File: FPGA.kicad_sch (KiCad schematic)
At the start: 1 part, among them U2 LFE5U-85F-6BG381x

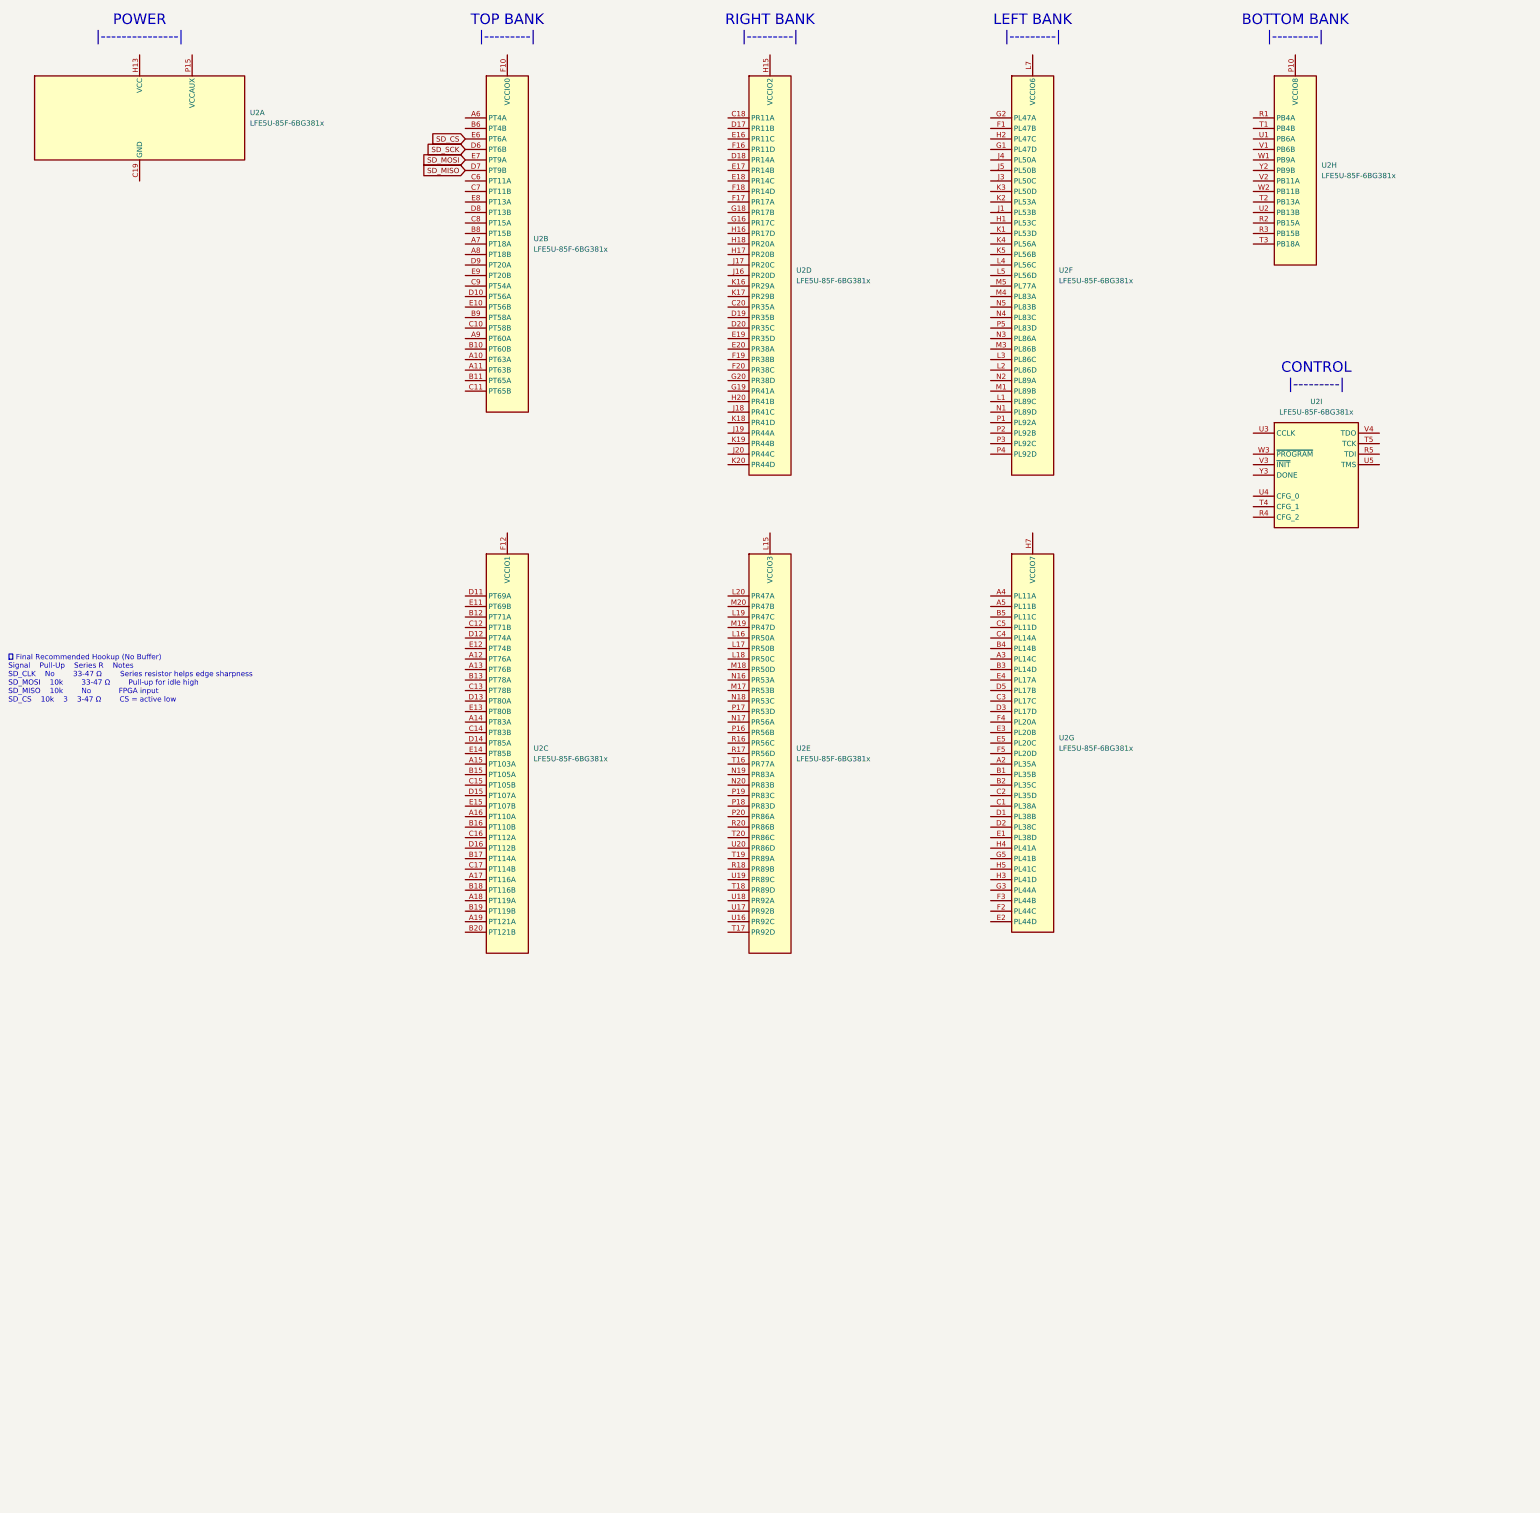
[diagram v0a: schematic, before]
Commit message: Changed power regulators, filled out DRAM, begin changing FPGA from ECP5 to ICE40
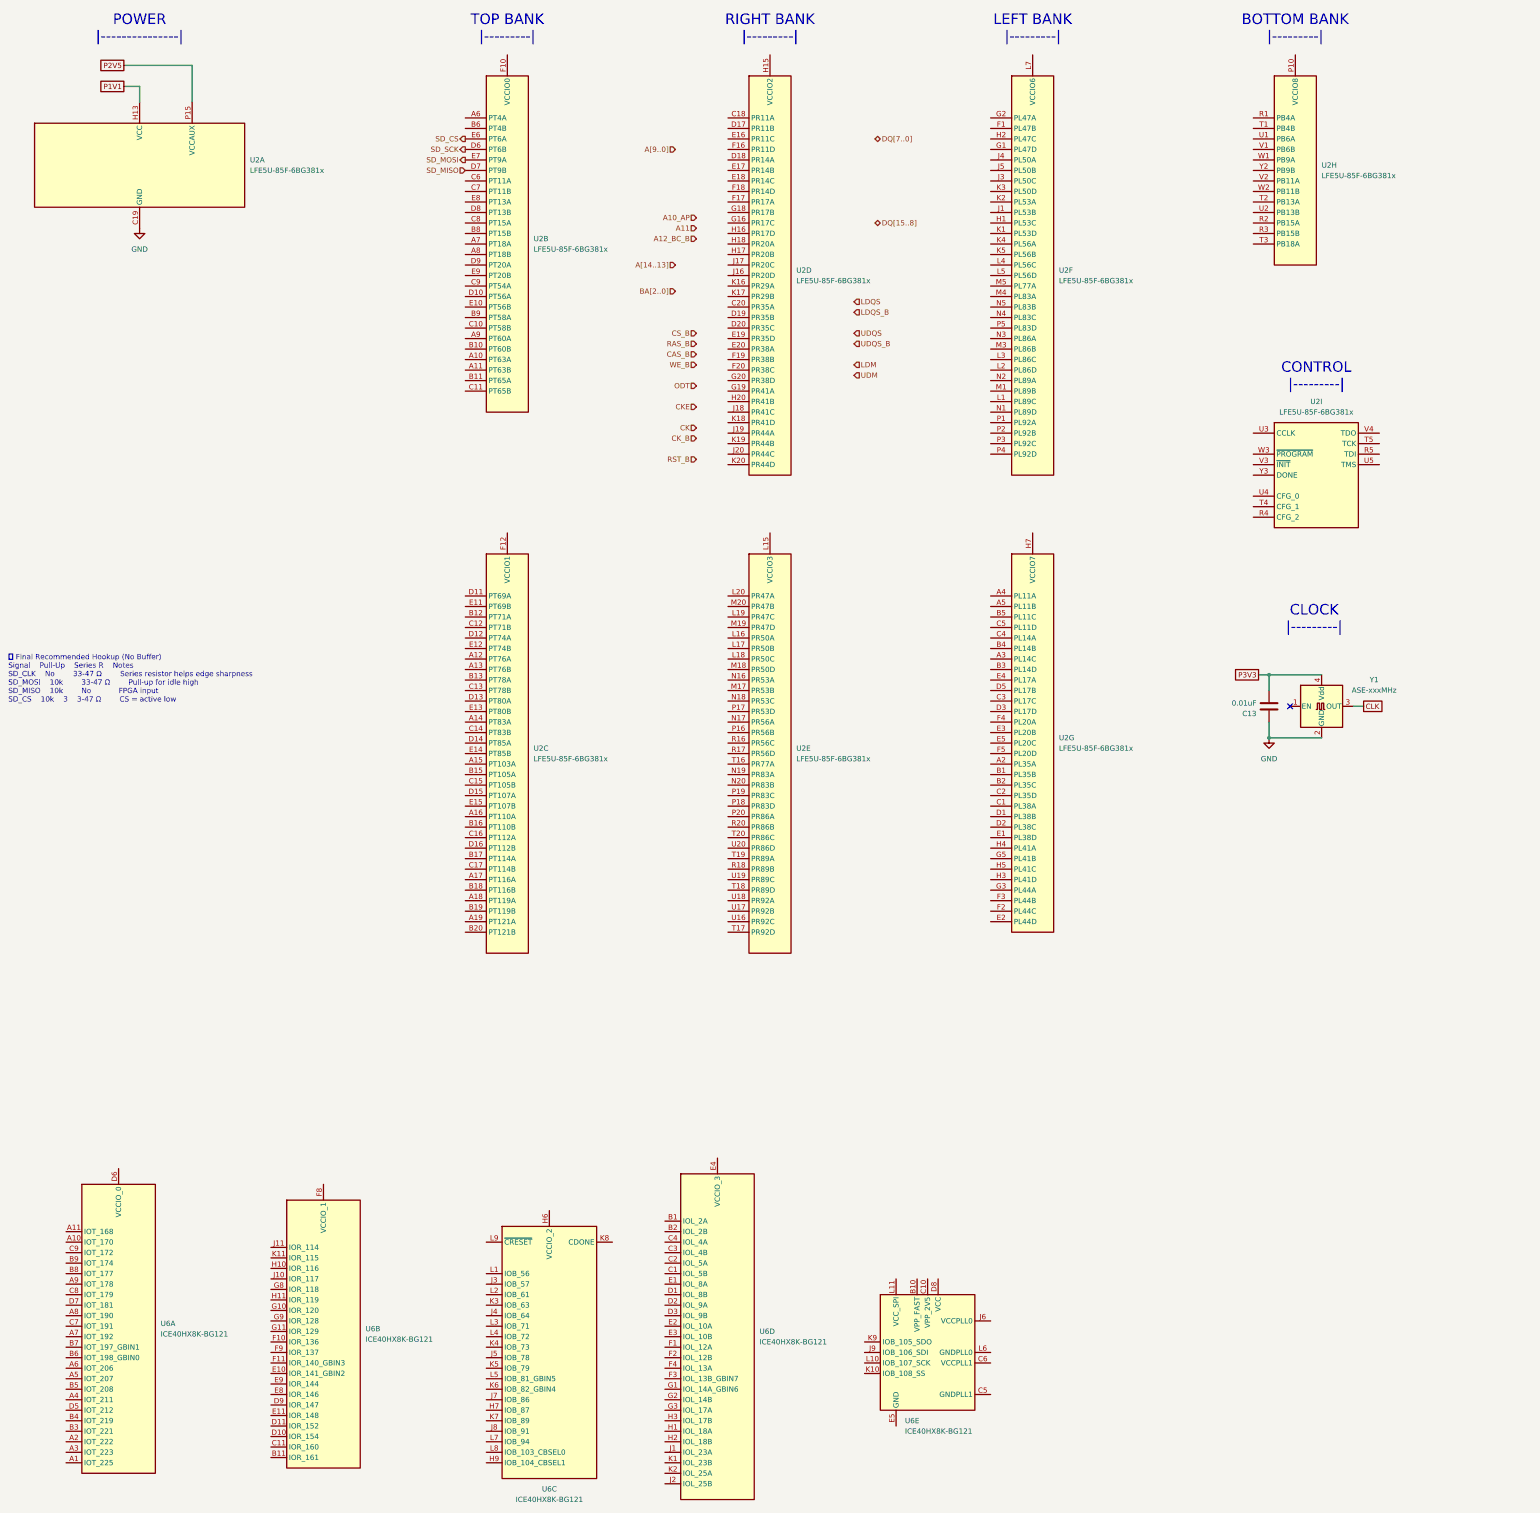
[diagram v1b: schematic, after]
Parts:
- added C13: 0.01uF, symbol Device:C
- added U6: ICE40HX8K-BG121, Package_BGA:BGA-121_9.0x9.0mm_Layout11x11_P0.8mm_Ball0.4mm_Pad0.35mm_NSMD, symbol FPGA_Lattice:ICE40HX8K-BG121
- added Y1: ASE-xxxMHz, Oscillator:Oscillator_SMD_Abracon_ASE-4Pin_3.2x2.5mm, symbol Oscillator:ASE-xxxMHz
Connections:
- net GND: now reaches U2.B14 (GND), U2.B7 (GND), U2.C19 (GND), U2.D4 (GND), U2.F13 (GND), U2.F14 (GND), U2.F7 (GND), U2.F8 (GND), U2.G10 (GND), U2.G11 (GND), U2.G12 (GND), U2.G13 (GND), U2.G14 (GND), U2.G15 (GND), U2.G17 (GND), U2.G4 (GND), U2.G6 (GND), U2.G7 (GND), U2.G8 (GND), U2.G9 (GND), U2.H19 (GND), U2.J10 (GND), U2.J11 (GND), U2.J12 (GND), U2.J14 (GND), U2.J2 (GND), U2.J7 (GND), U2.J9 (GND), U2.K10 (GND), U2.K11 (GND), U2.K12 (GND), U2.K14 (GND), U2.K15 (GND), U2.K6 (GND), U2.K7 (GND), U2.K9 (GND), U2.L10 (GND), U2.L11 (GND), U2.L12 (GND), U2.L9 (GND), U2.M10 (GND), U2.M11 (GND), U2.M12 (GND), U2.M14 (GND), U2.M16 (GND), U2.M2 (GND), U2.M7 (GND), U2.M9 (GND), U2.N14 (GND), U2.N15 (GND), U2.N6 (GND), U2.N7 (GND), U2.P11 (GND), U2.P12 (GND), U2.P13 (GND), U2.P14 (GND), U2.P7 (GND), U2.P8 (GND), U2.R19 (GND), U2.T10 (GND), U2.T11 (GND), U2.T12 (GND), U2.T13 (GND), U2.T14 (GND), U2.T15 (GND), U2.T6 (GND), U2.T7 (GND), U2.T8 (GND), U2.T9 (GND), U2.U10 (GND), U2.U11 (GND), U2.U12 (GND), U2.U13 (GND), U2.U14 (GND), U2.U15 (GND), U2.U6 (GND), U2.U7 (GND), U2.U8 (GND), U2.U9 (GND), U2.V10 (GND), U2.V11 (GND), U2.V12 (GND), U2.V13 (GND), U2.V14 (GND), U2.V15 (GND), U2.V16 (GND), U2.V17 (GND), U2.V18 (GND), U2.V19 (GND), U2.V20 (GND), U2.V5 (GND), U2.V6 (GND), U2.V7 (GND), U2.V8 (GND), U2.V9 (GND), U2.W12 (GND), U2.W15 (GND), U2.W16 (GND), U2.W19 (GND), U2.W20 (GND), U2.W6 (GND), U2.W7 (GND), U2.Y11 (GND), U2.Y12 (GND), U2.Y14 (GND), U2.Y15 (GND), U2.Y16 (GND), U2.Y17 (GND), U2.Y19 (GND), U2.Y5 (GND), U2.Y6 (GND), U2.Y7 (GND), U2.Y8 (GND)
- net GND: now also C13.2, Y1.2 (GND)
- net P2V5: now reaches U2.F15 (VCCAUX), U2.F6 (VCCAUX), U2.P15 (VCCAUX), U2.P6 (VCCAUX)
- net P1V1: now reaches U2.H10 (VCC), U2.H11 (VCC), U2.H12 (VCC), U2.H13 (VCC), U2.H8 (VCC), U2.H9 (VCC), U2.J13 (VCC), U2.J8 (VCC), U2.K13 (VCC), U2.K8 (VCC), U2.L13 (VCC), U2.L8 (VCC), U2.M13 (VCC), U2.M8 (VCC), U2.N10 (VCC), U2.N11 (VCC), U2.N12 (VCC), U2.N13 (VCC), U2.N8 (VCC), U2.N9 (VCC)
- new net: U6.E4 (VCCIO_3), U6.G4 (VCCIO_3)
- new net: U6.D4 (VCC), U6.D8 (VCC), U6.H4 (VCC), U6.H8 (VCC)
- new net: U6.E5 (GND), U6.E6 (GND), U6.E7 (GND), U6.F5 (GND), U6.F6 (GND), U6.F7 (GND), U6.G5 (GND), U6.G6 (GND), U6.G7 (GND), U6.H5 (GND)
- new net CLK: Y1.3 (OUT)
- new net P3V3: C13.1, Y1.4 (Vdd)
- no-connect marks 0 -> 1
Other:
- note added: "CLOCK |---------|"
- moved on the sheet: U2A

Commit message: Saving before changing RAM from DDR3 to Parallel SDR SRAM
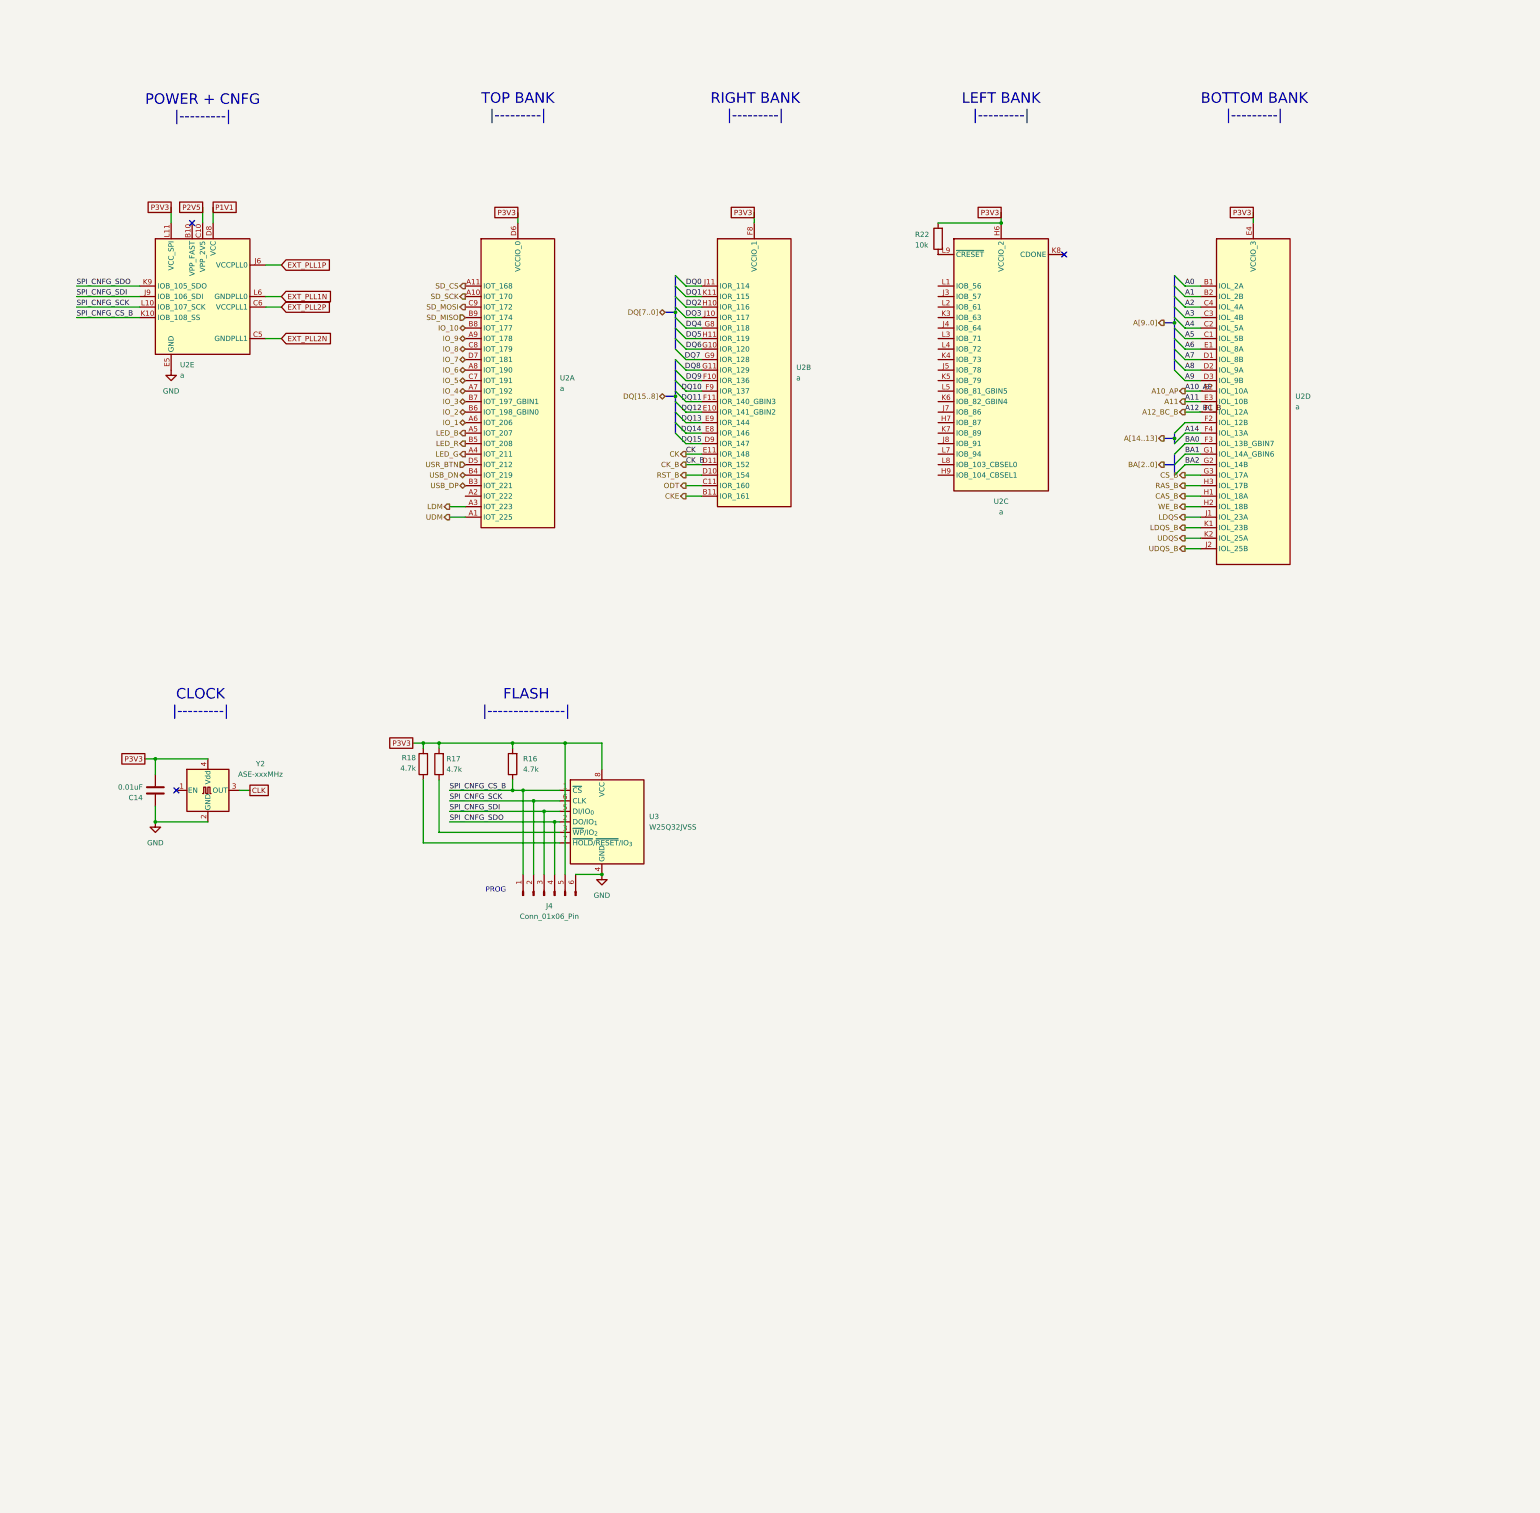
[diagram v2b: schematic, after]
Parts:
- removed U2: LFE5U-85F-6BG381x, Package_BGA:Lattice_caBGA-381_17.0x17.0mm_Layout20x20_P0.8mm_Ball0.4mm_Pad0.4mm_NSMD, symbol FPGA_Lattice:LFE5U-85F-6BG381x
- added J4: Conn_01x06_Pin, symbol Connector:Conn_01x06_Pin
- added R16, R17, R18: 4.7k, symbol Device:R
- added R22: 10k, symbol Device:R
- added U3: W25Q32JVSS, Package_SO:SOIC-8_5.3x5.3mm_P1.27mm, symbol Memory_Flash:W25Q32JVSS
- U2: renamed from U6; value ICE40HX8K-BG121 -> a
- renumbered C13 to C14, Y1 to Y2
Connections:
- net A10_AP: now also U2.E2 (IOL_10A)
- net A11: now also U2.E3 (IOL_10B)
- net A12_BC_B: now also U2.F1 (IOL_12A)
- net CAS_B: now also U2.H1 (IOL_18A)
- net CK: now also U2.E11 (IOR_148)
- net CKE: now also U2.B11 (IOR_161)
- net CK_B: now also U2.D11 (IOR_152)
- net CS_B: now also U2.G3 (IOL_17A)
- net GND: now also U2.E5 (GND), U2.E6 (GND), U2.E7 (GND), U2.F5 (GND), U2.F6 (GND), U2.F7 (GND), U2.G5 (GND), U2.G6 (GND), U2.G7 (GND), U2.H5 (GND), J4.6 (Pin_6), U3.4 (GND)
- net LDM: now also U2.A3 (IOT_223)
- net LDQS: now also U2.J1 (IOL_23A)
- net LDQS_B: now also U2.K1 (IOL_23B)
- net ODT: now also U2.C11 (IOR_160)
- net P1V1: now also U2.D4 (VCC), U2.D8 (VCC), U2.H4 (VCC), U2.H8 (VCC)
- net P2V5: now also U2.C10 (VPP_2V5)
- net P3V3: now also U2.D6 (VCCIO_0), U2.E4 (VCCIO_3), U2.F8 (VCCIO_1), U2.G4 (VCCIO_3), U2.H6 (VCCIO_2), U2.L11 (VCC_SPI), J4.5 (Pin_5), R16.2, R17.2, R18.2, R22.2, U3.8 (VCC)
- net RAS_B: now also U2.H3 (IOL_17B)
- net RST_B: now also U2.D10 (IOR_154)
- net SD_CS: now also U2.A11 (IOT_168)
- net SD_MISO: now also U2.B9 (IOT_174)
- net SD_MOSI: now also U2.C9 (IOT_172)
- net SD_SCK: now also U2.A10 (IOT_170)
- net UDM: now also U2.A1 (IOT_225)
- net UDQS: now also U2.K2 (IOL_25A)
- net UDQS_B: now also U2.J2 (IOL_25B)
- net WE_B: now also U2.H2 (IOL_18B)
- net LED_G: now reaches U2.A4 (IOT_211)
- net LED_B: now reaches U2.A5 (IOT_207)
- net IO_1: now reaches U2.A6 (IOT_206)
- net IO_4: now reaches U2.A7 (IOT_192)
- net IO_6: now reaches U2.A8 (IOT_190)
- net IO_9: now reaches U2.A9 (IOT_178)
- net USB_DP: now reaches U2.B3 (IOT_221)
- net USB_DN: now reaches U2.B4 (IOT_219)
- net LED_R: now reaches U2.B5 (IOT_208)
- net IO_2: now reaches U2.B6 (IOT_198_GBIN0)
- net IO_3: now reaches U2.B7 (IOT_197_GBIN1)
- net IO_10: now reaches U2.B8 (IOT_177)
- net IO_5: now reaches U2.C7 (IOT_191)
- net IO_8: now reaches U2.C8 (IOT_179)
- net USR_BTN: now reaches U2.D5 (IOT_212)
- net IO_7: now reaches U2.D7 (IOT_181)
- net DQ15: now reaches U2.D9 (IOR_147)
- net DQ12: now reaches U2.E10 (IOR_141_GBIN2)
- net DQ14: now reaches U2.E8 (IOR_146)
- net DQ13: now reaches U2.E9 (IOR_144)
- net DQ9: now reaches U2.F10 (IOR_136)
- net DQ11: now reaches U2.F11 (IOR_140_GBIN3)
- net DQ10: now reaches U2.F9 (IOR_137)
- net DQ6: now reaches U2.G10 (IOR_120)
- net DQ8: now reaches U2.G11 (IOR_129)
- net DQ4: now reaches U2.G8 (IOR_118)
- net DQ7: now reaches U2.G9 (IOR_128)
- net DQ2: now reaches U2.H10 (IOR_116)
- net DQ5: now reaches U2.H11 (IOR_119)
- net DQ3: now reaches U2.J10 (IOR_117)
- net DQ0: now reaches U2.J11 (IOR_114)
- net DQ1: now reaches U2.K11 (IOR_115)
- net at U2.L9 (~{CRESET}): now also R22.1
- net A0: now reaches U2.B1 (IOL_2A)
- net A1: now reaches U2.B2 (IOL_2B)
- net A5: now reaches U2.C1 (IOL_5B)
- net A4: now reaches U2.C2 (IOL_5A)
- net A3: now reaches U2.C3 (IOL_4B)
- net A2: now reaches U2.C4 (IOL_4A)
- net A7: now reaches U2.D1 (IOL_8B)
- net A8: now reaches U2.D2 (IOL_9A)
- net A9: now reaches U2.D3 (IOL_9B)
- net A6: now reaches U2.E1 (IOL_8A)
- net BA0: now reaches U2.F3 (IOL_13B_GBIN7)
- net A14: now reaches U2.F4 (IOL_13A)
- net BA1: now reaches U2.G1 (IOL_14A_GBIN6)
- net BA2: now reaches U2.G2 (IOL_14B)
- net EXT_PLL2N: now reaches U2.C5 (GNDPLL1)
- net EXT_PLL2P: now reaches U2.C6 (VCCPLL1)
- net EXT_PLL1P: now reaches U2.J6 (VCCPLL0)
- net SPI_CNFG_SDI: now reaches U2.J9 (IOB_106_SDI)
- net SPI_CNFG_SDI: now also J4.3 (Pin_3), U3.5 (DI/IO_{0})
- net SPI_CNFG_CS_B: now reaches U2.K10 (IOB_108_SS)
- net SPI_CNFG_CS_B: now also J4.1 (Pin_1), R16.1, U3.1 (~{CS})
- net SPI_CNFG_SDO: now reaches U2.K9 (IOB_105_SDO)
- net SPI_CNFG_SDO: now also J4.4 (Pin_4), U3.2 (DO/IO_{1})
- net SPI_CNFG_SCK: now reaches U2.L10 (IOB_107_SCK)
- net SPI_CNFG_SCK: now also J4.2 (Pin_2), U3.6 (CLK)
- net EXT_PLL1N: now reaches U2.L6 (GNDPLL0)
- new net: R18.1, U3.7 (~{HOLD}/~{RESET}/IO_{3})
- new net: R17.1, U3.3 (~{WP}/IO_{2})
- no-connect marks 1 -> 3
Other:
- note added: "FLASH |---------------|"
- note added: "POWER + CNFG |---------|"
- note added: "PROG"
- note removed: "CONTROL |---------|"
- note removed: "POWER |---------------|"
- note removed: "📋 Final Recommended Hookup (No Buffer) Signal Pull-Up Series R Notes SD_CLK No 33-47 Ω Series resistor helps edge sharpness SD_MOSI 10k 33-47 Ω Pull-up for idle high SD_MISO 10k No FPGA input SD_CS 10k 3 3-47 Ω CS = active low"
- moved on the sheet: C14, U2A, U2B, U2C, U2D, U2E, Y2
